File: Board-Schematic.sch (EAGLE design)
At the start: 18 parts, among them IC1 74HC595N, IC2 74HC595N, IC3 74HC595N

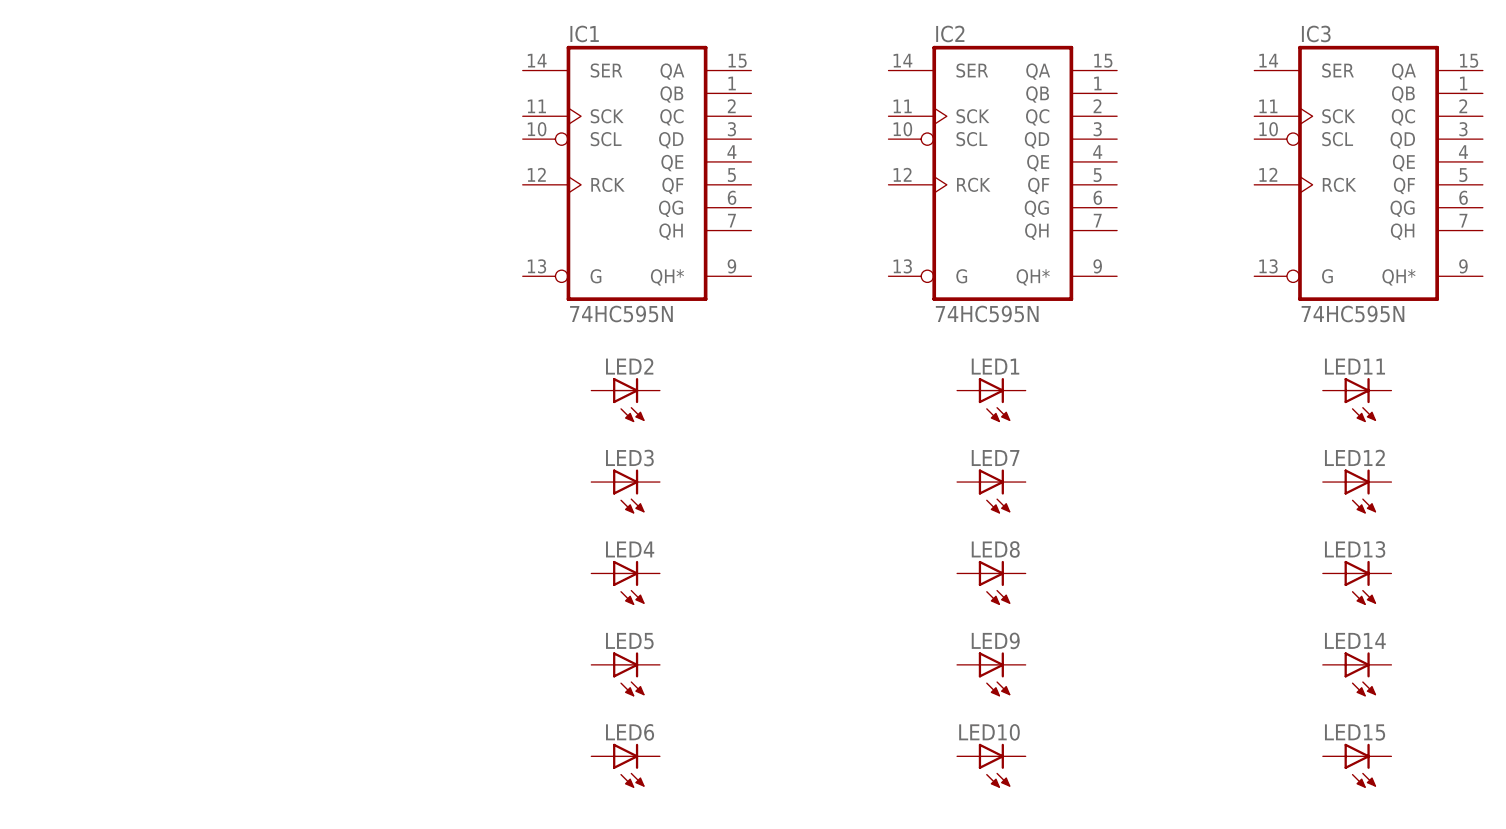
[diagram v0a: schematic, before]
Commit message: Schematic and quick board layout
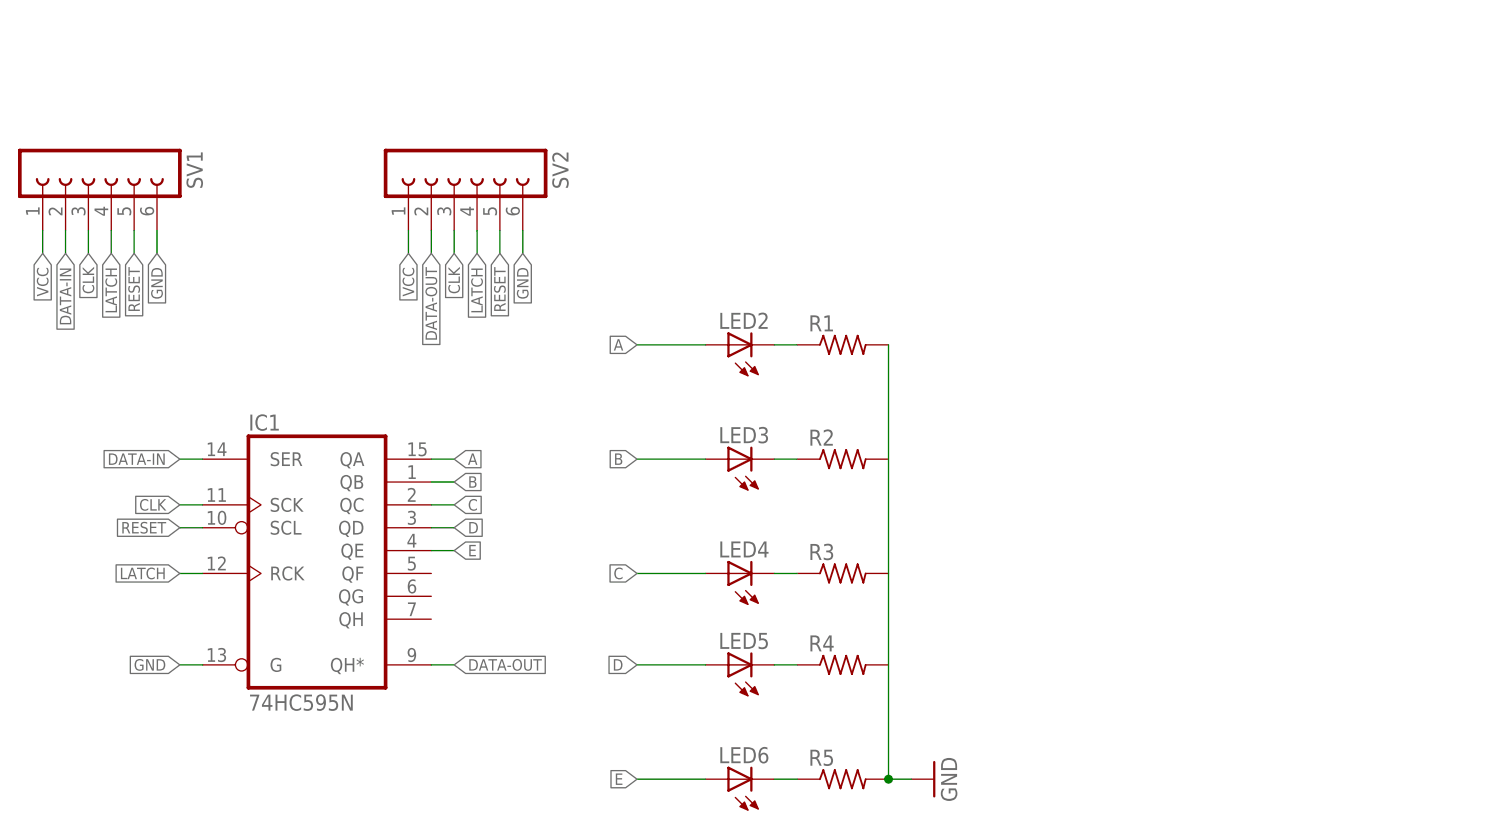
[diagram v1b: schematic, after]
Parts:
- removed IC2, IC3: 74HC595N, 74xx-eu:74HC595N
- removed LED1, LED10, LED11, LED12, LED13, LED14, LED15, LED7, LED8, LED9: (no value), led:LED5MM
- added R1, R2, R3, R4, R5: (no value), resistor:R-US_0204/7
- added SV1, SV2: (no value), con-lsta:FE06-1
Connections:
- new net A: IC1A.QA, LED2.A
- new net B: IC1A.QB, LED3.A
- new net C: IC1A.QC, LED4.A
- new net CLK: IC1A.SCK, SV1.3, SV2.3
- new net D: IC1A.QD, LED5.A
- new net DATA-IN: IC1A.SER, SV1.2
- new net DATA-OUT: IC1A.QH*, SV2.2
- new net E: IC1A.QE, LED6.A
- new net GND: IC1A.G, R1.2, R5.2, SV1.6, SV2.6
- new net LATCH: IC1A.RCK, SV1.4, SV2.4
- new net N$1: LED2.C, R1.1
- new net N$2: LED3.C, R2.1
- new net N$3: LED4.C, R3.1
- new net N$4: LED5.C, R4.1
- new net N$5: LED6.C, R5.1
- new net RESET: IC1A.SCL, SV1.5, SV2.5
- new net VCC: SV1.1, SV2.1
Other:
- moved on the sheet: IC1, LED2, LED3, LED4, LED5, LED6
